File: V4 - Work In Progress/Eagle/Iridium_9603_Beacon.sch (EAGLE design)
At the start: 77 parts, among them CON4 uFL, J1 SS4-10-3.50-X-D, Q1 DMG3415U-7, U1 MCP111T-240E/TT, U2 SPX3819-3.3, U3 LTC3225EDDB#TRMPBF, U4 MPL3115A2LGA8, U5 ATSAMD21G18_QFN, U6 MAX-M8, U7 LT1634-1,25BMCMS8, X1 32.768

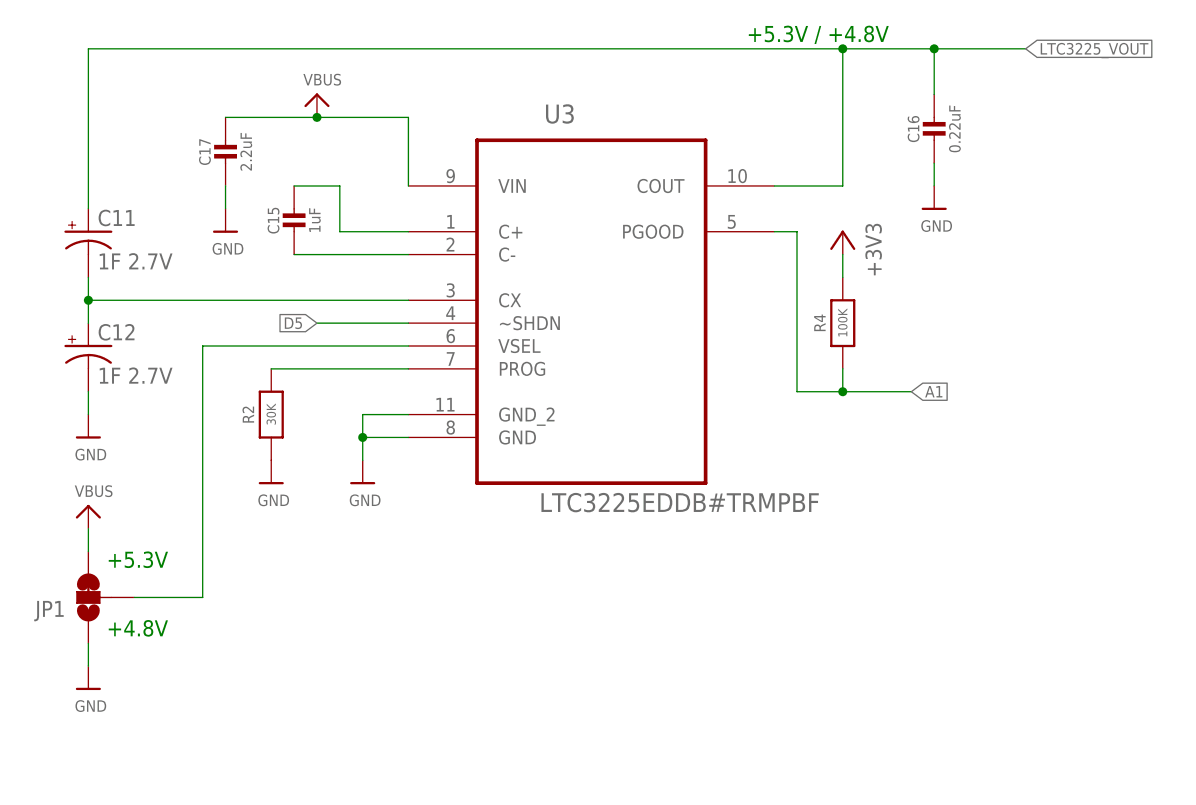
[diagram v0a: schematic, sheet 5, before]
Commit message: Added split pads for supercapacitor charge current
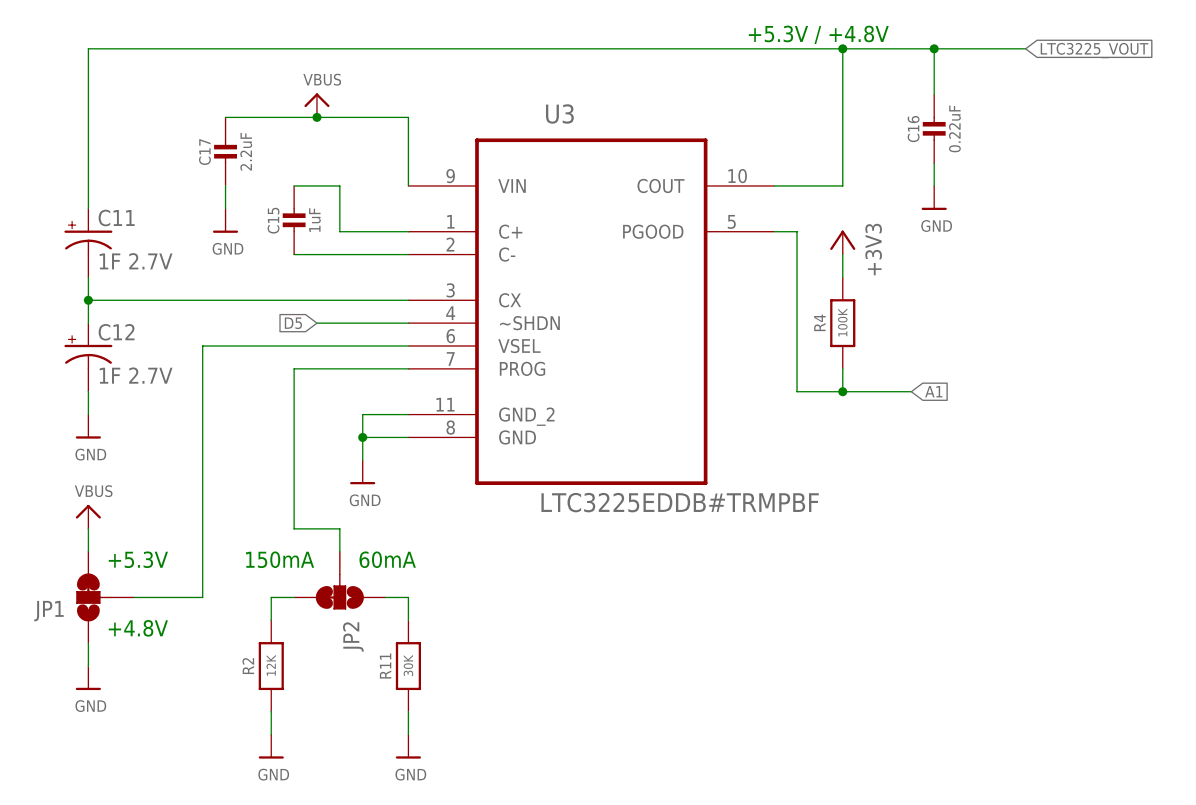
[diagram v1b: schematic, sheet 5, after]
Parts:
- added JP2: JUMPER-PAD-3-2OF3_NC_BY_TRACE_LARGE, SparkFun-Passives:JUMPER-PAD-3-2OF3_NC_BY_TRACE_LARGE
- added R11: 30K, microbuilder:RESISTOR0805_NOOUTLINE
- R2: value 30K -> 12K
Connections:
- new net N$17: JP2.3, R2.2
- new net N$18: JP2.1, R11.2
- net GND: now also R11.1
- net N$11: now also JP2.2; no longer R2.2
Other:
- note added: "150mA"
- note added: "60mA"
- note added: "V4: Power: 3 x AA batteries in Keystone 92 clips GNSS: u-blox MAX-M8Q with SMA antenna Added WS2812B LED Added LT1634-1,25BMCMS8 voltage reference to allow low battery voltages to be measured SMA antenna for 9603N Added protection diode for USB power Added split pad to select supercapacitor charge current"
- note removed: "V4: Power: 3 x AA batteries in Keystone 92 clips GNSS: u-blox MAX-M8Q with SMA antenna WS2812B LED LT1634-1,25BMCMS8 voltage reference to allow low battery voltages to be measured SMA antenna for 9603N"
- moved on the sheet: R2
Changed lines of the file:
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@@
 <?xml version="1.0" encoding="utf-8"?>
 <!DOCTYPE eagle SYSTEM "eagle.dtd">
-<eagle version="8.5.0">
+<eagle version="8.6.0">
 <drawing>
 <settings>
@@
 <part name="U3" library="LTC_By_element14_Batch_1" deviceset="LTC3225EDDB-TRMPBF" device="DFN300X200-10L" value="LTC3225EDDB#TRMPBF"/>
 <part name="C15" library="microbuilder" deviceset="CAP_CERAMIC" device="0603_NO" value="1uF"/>
-<part name="R2" library="microbuilder" deviceset="RESISTOR" device="0805_NOOUTLINE" value="30K"/>
+<part name="R2" library="microbuilder" deviceset="RESISTOR" device="0805_NOOUTLINE" value="12K"/>
 <part name="U$20" library="microbuilder" deviceset="GND" device=""/>
 <part name="U$22" library="microbuilder" deviceset="GND" device=""/>
@@
 <part name="U$45" library="microbuilder" deviceset="VBUS" device=""/>
 <part name="D4" library="microbuilder" deviceset="DIODE-SCHOTTKY" device="SOD-123" value="MBR120"/>
+<part name="JP2" library="SparkFun-Passives" deviceset="JUMPER-PAD-3-2OF3_NC_BY_TRACE" device="_LARGE" value=""/>
+<part name="R11" library="microbuilder" deviceset="RESISTOR" device="0805_NOOUTLINE" value="30K"/>
+<part name="U$1" library="microbuilder" deviceset="GND" device=""/>
 </parts>
 <sheets>
@@
 <text x="70.612" y="84.582" size="1.778" layer="91">+5.3V</text>
 <text x="70.612" y="76.962" size="1.778" layer="91">+4.8V</text>
+<text x="85.852" y="84.582" size="1.778" layer="91">150mA</text>
+<text x="98.552" y="84.582" size="1.778" layer="91">60mA</text>
 </plain>
 <instances>
@@
 <instance part="U3" gate="G$1" x="124.46" y="116.84"/>
 <instance part="C15" gate="G$1" x="91.44" y="121.92"/>
-<instance part="R2" gate="G$1" x="88.9" y="101.6" rot="R90"/>
-<instance part="U$20" gate="G$1" x="88.9" y="93.98"/>
+<instance part="R2" gate="G$1" x="88.9" y="73.66" rot="R90"/>
+<instance part="U$20" gate="G$1" x="88.9" y="63.5"/>
 <instance part="U$22" gate="G$1" x="99.06" y="93.98"/>
 <instance part="U$23" gate="G$1" x="68.58" y="99.06"/>
@@
 <instance part="U$26" gate="G$1" x="68.58" y="91.44"/>
 <instance part="U$32" gate="G$1" x="68.58" y="71.12"/>
+<instance part="JP2" gate="G$1" x="96.52" y="81.28" rot="R270"/>
+<instance part="R11" gate="G$1" x="104.14" y="73.66" rot="R90"/>
+<instance part="U$1" gate="G$1" x="104.14" y="63.5"/>
 </instances>
 <busses>
@@
 <pinref part="R2" gate="G$1" pin="1"/>
 <pinref part="U$20" gate="G$1" pin="GND"/>
+<wire x1="88.9" y1="66.04" x2="88.9" y2="68.58" width="0.1524" layer="91"/>
 </segment>
 <segment>
@@
 <wire x1="68.58" y1="73.66" x2="68.58" y2="76.2" width="0.1524" layer="91"/>
 </segment>
-</net>
-<net name="N$11" class="0">
-<segment>
-<pinref part="U3" gate="G$1" pin="PROG"/>
-<pinref part="R2" gate="G$1" pin="2"/>
-<wire x1="104.14" y1="106.68" x2="88.9" y2="106.68" width="0.1524" layer="91"/>
+<segment>
+<pinref part="R11" gate="G$1" pin="1"/>
+<pinref part="U$1" gate="G$1" pin="GND"/>
+<wire x1="104.14" y1="68.58" x2="104.14" y2="66.04" width="0.1524" layer="91"/>
 </segment>
 </net>
@@
 <pinref part="JP1" gate="G$1" pin="2"/>
 <wire x1="81.28" y1="81.28" x2="73.66" y2="81.28" width="0.1524" layer="91"/>
+</segment>
+</net>
+<net name="N$11" class="0">
+<segment>
+<pinref part="U3" gate="G$1" pin="PROG"/>
+<wire x1="104.14" y1="106.68" x2="91.44" y2="106.68" width="0.1524" layer="91"/>
+<wire x1="91.44" y1="106.68" x2="91.44" y2="88.9" width="0.1524" layer="91"/>
+<wire x1="91.44" y1="88.9" x2="96.52" y2="88.9" width="0.1524" layer="91"/>
+<pinref part="JP2" gate="G$1" pin="2"/>
+<wire x1="96.52" y1="88.9" x2="96.52" y2="86.36" width="0.1524" layer="91"/>
+</segment>
+</net>
+<net name="N$17" class="0">
+<segment>
+<pinref part="JP2" gate="G$1" pin="3"/>
+<wire x1="91.44" y1="81.28" x2="88.9" y2="81.28" width="0.1524" layer="91"/>
+<pinref part="R2" gate="G$1" pin="2"/>
+<wire x1="88.9" y1="81.28" x2="88.9" y2="78.74" width="0.1524" layer="91"/>
+</segment>
+</net>
+<net name="N$18" class="0">
+<segment>
+<pinref part="JP2" gate="G$1" pin="1"/>
+<wire x1="101.6" y1="81.28" x2="104.14" y2="81.28" width="0.1524" layer="91"/>
+<pinref part="R11" gate="G$1" pin="2"/>
+<wire x1="104.14" y1="81.28" x2="104.14" y2="78.74" width="0.1524" layer="91"/>
 </segment>
 </net>
@@
 Power: 3 x AA batteries in Keystone 92 clips
 GNSS: u-blox MAX-M8Q with SMA antenna
-WS2812B LED
-LT1634-1,25BMCMS8 voltage reference to allow low battery voltages to be measured
+Added WS2812B LED
+Added LT1634-1,25BMCMS8 voltage reference to allow low battery voltages to be measured
 SMA antenna for 9603N
+Added protection diode for USB power
+Added split pad to select supercapacitor charge current
 </text>
 </plain>
@@
 Solar panel must not produce more than 6V (open circuit) under full sun.
 (Quoted open circuit voltage for PowerFilm Solar MPT3.6-150 is 4.8V)
-BUT! Don't forget that VBUS is connected directly to the USB port. If VBUS is higher than 5V, it will attempt to
-deliver power to anything connected to the USB port. For safety, always use a USB Power Break cable if
-there is any chance of VBUS going higher than 5V. (Three new Energiser cells will deliver approx. 5.4V)
 </text>
 </plain>

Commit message: Minor tweaks
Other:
- note added: "V4: Power: 3 x AA batteries in Keystone 92 clips GNSS: u-blox MAX-M8Q with SMA antenna SMA antenna for 9603N Added WS2812B LED Added LT1634-1,25BMCMS8 voltage reference to allow low battery voltages to be measured Added protection diode for USB power Added split pad to select supercapacitor charge current"
- note removed: "V4: Power: 3 x AA batteries in Keystone 92 clips GNSS: u-blox MAX-M8Q with SMA antenna Added WS2812B LED Added LT1634-1,25BMCMS8 voltage reference to allow low battery voltages to be measured SMA antenna for 9603N Added protection diode for USB power Added split pad to select supercapacitor charge current"
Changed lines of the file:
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@@
 Power: 3 x AA batteries in Keystone 92 clips
 GNSS: u-blox MAX-M8Q with SMA antenna
+SMA antenna for 9603N
 Added WS2812B LED
 Added LT1634-1,25BMCMS8 voltage reference to allow low battery voltages to be measured
-SMA antenna for 9603N
 Added protection diode for USB power
 Added split pad to select supercapacitor charge current
